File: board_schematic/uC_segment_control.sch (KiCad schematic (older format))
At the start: 61 parts, among them IC1 ATMEGA88PA-P, P1 CONN_02X05

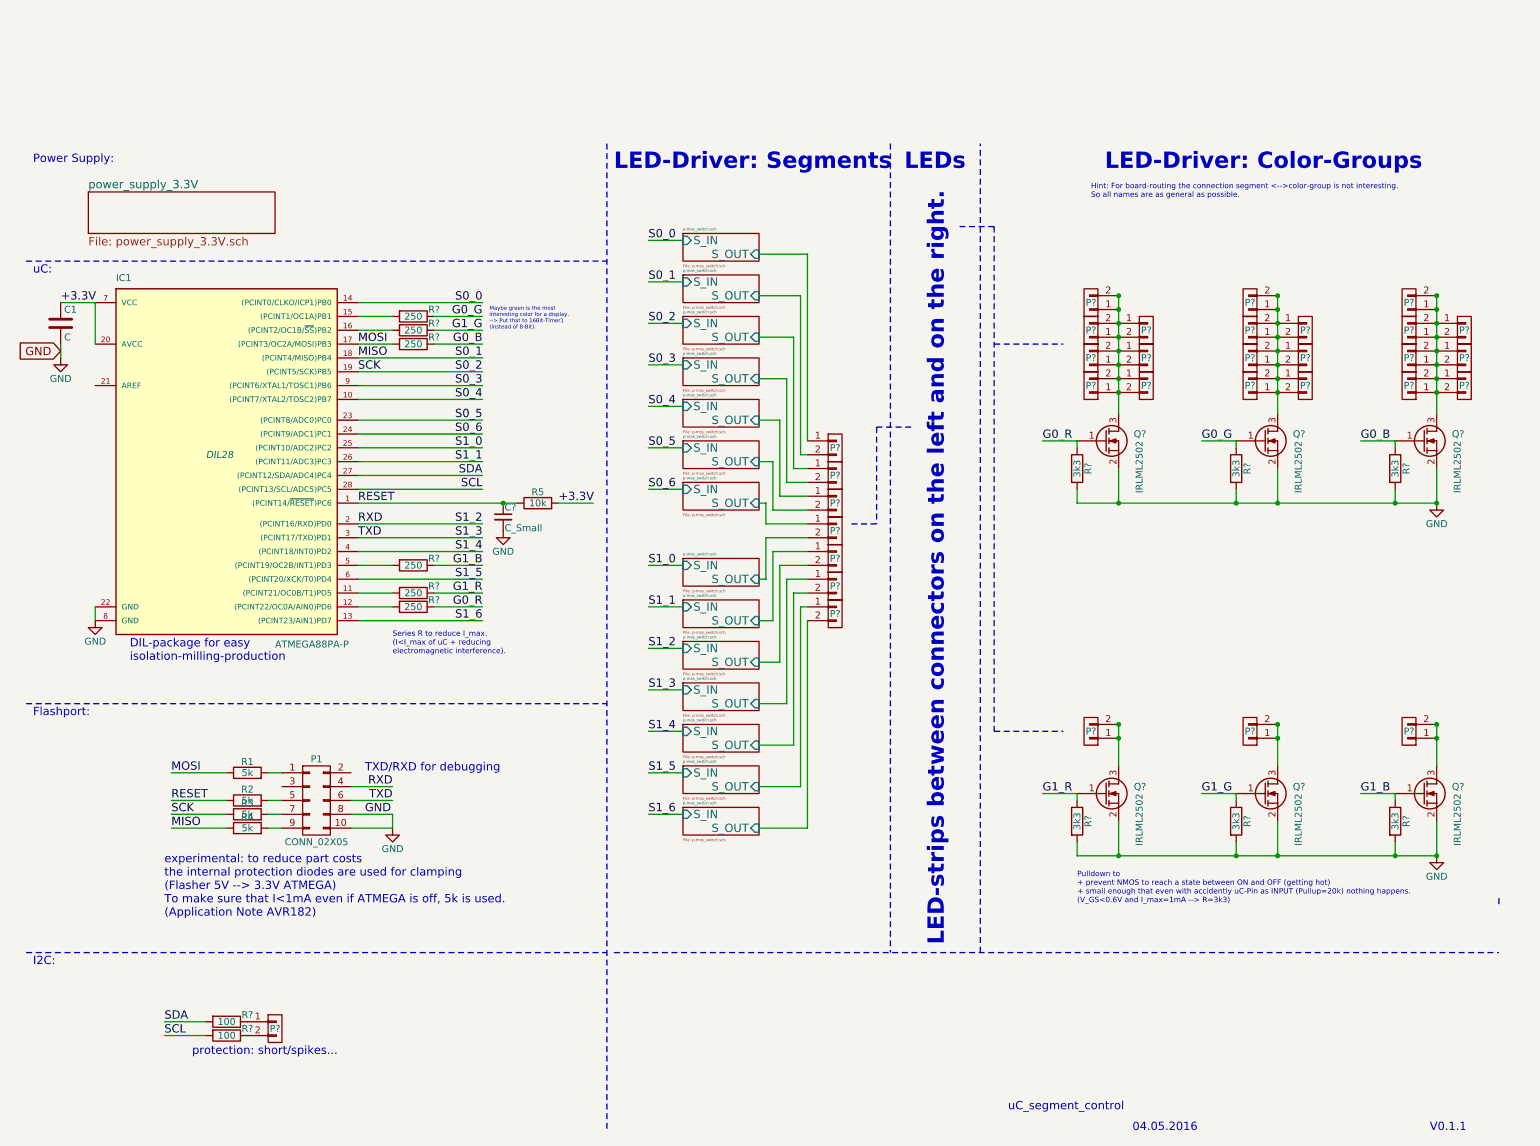
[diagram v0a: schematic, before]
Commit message: V0.2.1: First schematic for BOM
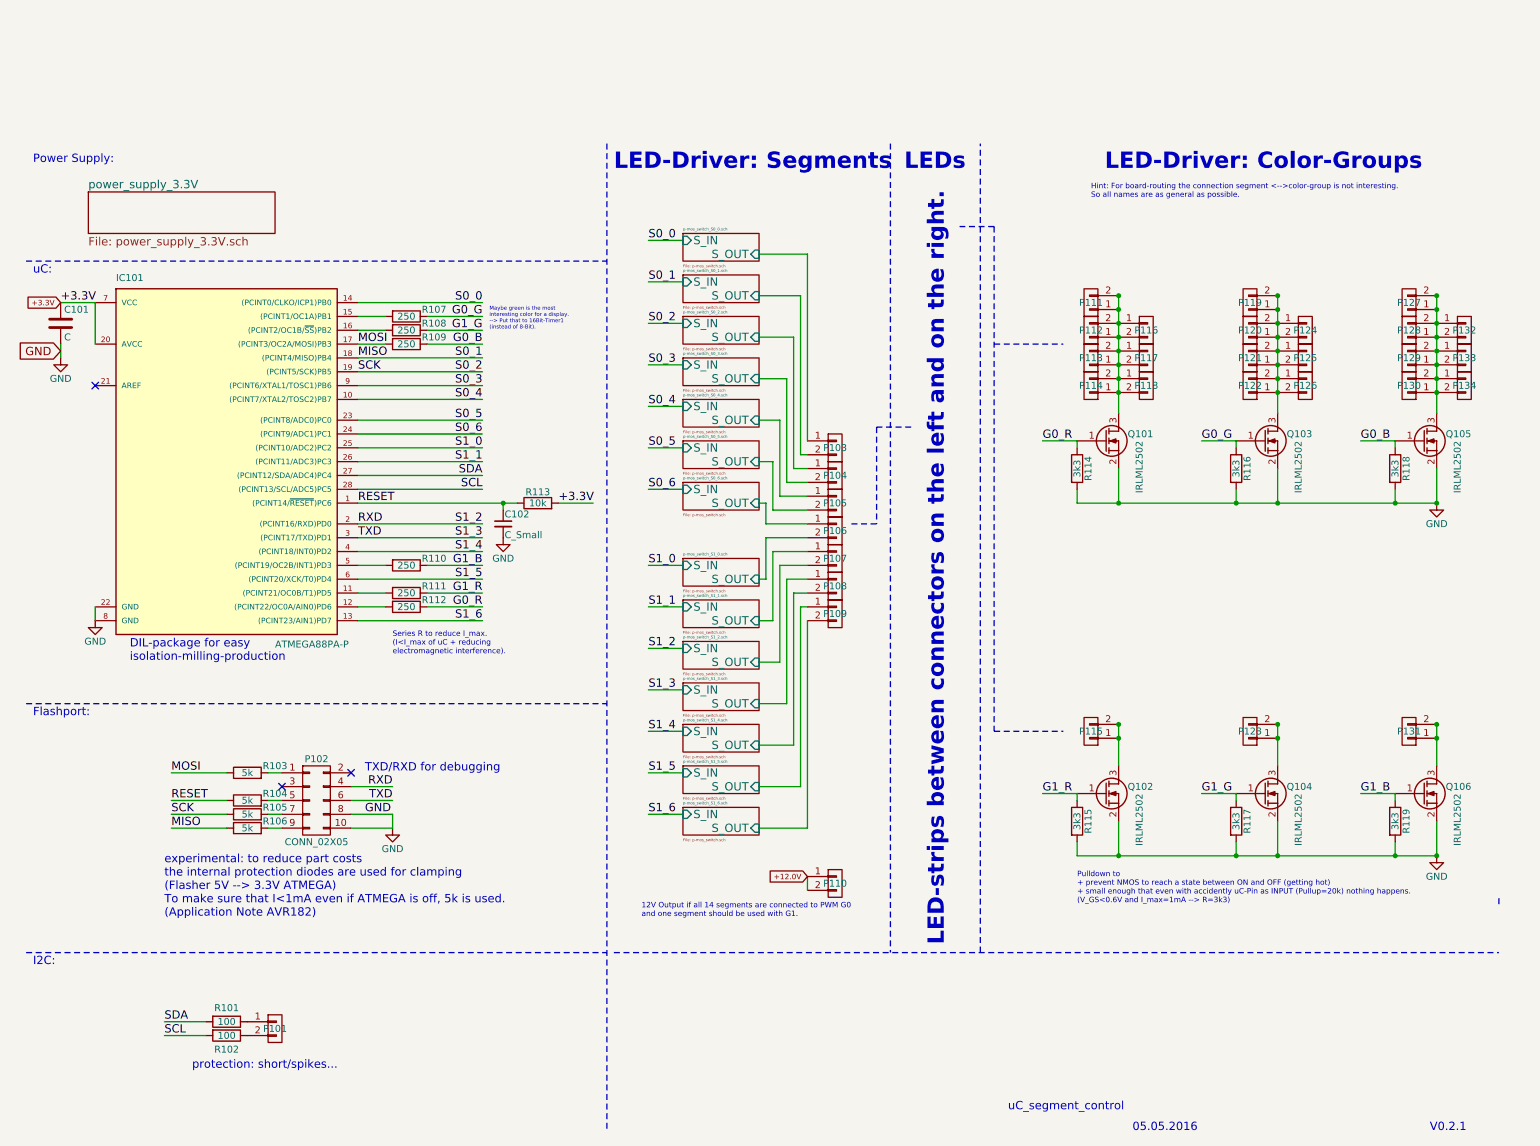
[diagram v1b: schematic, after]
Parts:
- added P110: CONN_01X02, Connect:bornier2, symbol CONN_01X02
- C101: renamed from C1; footprint (none) -> Capacitors_SMD:C_0805_HandSoldering
- C102: renamed from C?; footprint (none) -> Capacitors_SMD:C_0805_HandSoldering
- IC101: renamed from IC1; footprint DIL28 -> Housings_DIP:DIP-28_W7.62mm_LongPads
- P101, P103, P104, P105, P106, P107, P108, P109, P111, P112, P113, P114, P115, P116, P117, P118, P119, P120, P121, P122, P123, P124, P125, P126, P127, P128, P129, P130, P131, P132, P133, P134: renamed from P?; footprint (none) -> Connect:bornier2
- Q101, Q102, Q103, Q104, Q105, Q106: renamed from Q?; footprint (none) -> TO_SOT_Packages_SMD:SOT-23_Handsoldering
- gave numbers to parts that had none: 14
- renumbered P1 to P102, R1 to R103, R2 to R104, R3 to R105, R4 to R106, R5 to R113
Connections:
- net p-mos_switch.sch/S_OUT renamed p-mos_switch_S1_5.sch/S_OUT
- net p-mos_switch.sch/S_OUT renamed p-mos_switch_S1_6.sch/S_OUT
- net p-mos_switch.sch/S_OUT renamed p-mos_switch_S1_3.sch/S_OUT
- net p-mos_switch.sch/S_OUT renamed p-mos_switch_S1_4.sch/S_OUT
- net p-mos_switch.sch/S_OUT renamed p-mos_switch_S1_1.sch/S_OUT
- net p-mos_switch.sch/S_OUT renamed p-mos_switch_S1_2.sch/S_OUT
- net p-mos_switch.sch/S_OUT renamed p-mos_switch_S0_6.sch/S_OUT
- net p-mos_switch.sch/S_OUT renamed p-mos_switch_S1_0.sch/S_OUT
- net p-mos_switch.sch/S_OUT renamed p-mos_switch_S0_4.sch/S_OUT
- net p-mos_switch.sch/S_OUT renamed p-mos_switch_S0_5.sch/S_OUT
- net p-mos_switch.sch/S_OUT renamed p-mos_switch_S0_2.sch/S_OUT
- net p-mos_switch.sch/S_OUT renamed p-mos_switch_S0_3.sch/S_OUT
- net p-mos_switch.sch/S_OUT renamed p-mos_switch_S0_0.sch/S_OUT
- net p-mos_switch.sch/S_OUT renamed p-mos_switch_S0_1.sch/S_OUT
- new net +12.0V: P110.1 (P1), P110.2 (P2)
- no-connect marks 0 -> 3
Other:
- note added: "05.05.2016"
- note added: "12V Output if all 14 segments are connected to PWM G0\nand one segment should be used with G1."
- note added: "V0.2.1"
- note removed: "04.05.2016"
- note removed: "V0.1.1"
- moved on the sheet: C102, R107, R108, R109, R110, R111, R112

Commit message: V0.3.1: First layout
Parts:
- removed P105, P106, P107, P111, P112, P113, P119, P120, P121, P127, P128, P129: CONN_01X02, Connect:bornier2, symbol CONN_01X02
- added P101, P102, P103, P104, P105, P106, P121, P122: CONN_01X03, Connect:AK300-3, symbol CONN_01X03
- added R112, R114: 5k, Resistors_SMD:R_0805_HandSoldering, symbol R
- C101: value C -> 100n
- C102: value C_Small -> 100n
- P107: renamed from P116; footprint Connect:bornier2 -> Connect:AK300-2
- P108: renamed from P117; footprint Connect:bornier2 -> Connect:AK300-2
- P109: renamed from P124; footprint Connect:bornier2 -> Connect:AK300-2
- P110: renamed from P125; footprint Connect:bornier2 -> Connect:AK300-2
- P111: renamed from P132; footprint Connect:bornier2 -> Connect:AK300-2
- P112: renamed from P133; footprint Connect:bornier2 -> Connect:AK300-2
- P113: renamed from P114; footprint Connect:bornier2 -> Connect:AK300-2
- P114: renamed from P118; footprint Connect:bornier2 -> Connect:AK300-2
- P115: renamed from P122; footprint Connect:bornier2 -> Connect:AK300-2
- P116: renamed from P126; footprint Connect:bornier2 -> Connect:AK300-2
- P117: renamed from P130; footprint Connect:bornier2 -> Connect:AK300-2
- P118: renamed from P134; footprint Connect:bornier2 -> Connect:AK300-2
- P119: renamed from P103; footprint Connect:bornier2 -> Connect:AK300-2
- P120: renamed from P104; footprint Connect:bornier2 -> Connect:AK300-2
- P123: renamed from P108; footprint Connect:bornier2 -> Connect:AK300-2
- P124: renamed from P109; footprint Connect:bornier2 -> Connect:AK300-2
- P125: renamed from P115; footprint Connect:bornier2 -> Connect:AK300-2
- P126: renamed from P123; footprint Connect:bornier2 -> Connect:AK300-2
- P127: renamed from P131; footprint Connect:bornier2 -> Connect:AK300-2
- P129: renamed from P110; footprint Connect:bornier2 -> Connect:AK300-2
- P130: renamed from P101; footprint Connect:bornier2 -> Connect:AK300-2
- R101: renamed from R107; value 250 -> 270
- R102: renamed from R108; value 250 -> 270
- R103: renamed from R109; value 250 -> 270
- R108: renamed from R110; value 250 -> 270
- R109: renamed from R111; value 250 -> 270
- R110: renamed from R112; value 250 -> 270
- renumbered P102 to P128, Q103 to Q102, Q105 to Q103, Q102 to Q104, Q104 to Q105, R114 to R104, R116 to R105, R118 to R106, R113 to R107, R103 to R111, R104 to R113, R105 to R115, R115 to R116, R119 to R118, R106 to R119, R101 to R120, R102 to R121
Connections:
- net RXD: now also R112.2; no longer P128.4 (P4)
- net S1_3: now also R114.2; no longer P128.6 (P6)
- net p-mos_switch_S0_4.sch/S_OUT: now also P121.1 (P1)
- net p-mos_switch_S0_5.sch/S_OUT: now also P121.2 (P2)
- net p-mos_switch_S0_6.sch/S_OUT: now also P121.3 (P3)
- net p-mos_switch_S1_0.sch/S_OUT: now also P122.1 (P1)
- net p-mos_switch_S1_1.sch/S_OUT: now also P122.2 (P2)
- net p-mos_switch_S1_2.sch/S_OUT: now also P122.3 (P3)
- net at P107.1 (P1), P107.2 (P2), P108.1 (P1)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: now also P101.1 (P1), P101.2 (P2), P101.3 (P3), P102.1 (P1), P102.2 (P2), P102.3 (P3)
- net at P109.1 (P1), P109.2 (P2), P110.1 (P1)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: now also P103.1 (P1), P103.2 (P2), P103.3 (P3), P104.1 (P1), P104.2 (P2), P104.3 (P3)
- net at P111.1 (P1), P111.2 (P2), P112.1 (P1)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: now also P105.1 (P1), P105.2 (P2), P105.3 (P3), P106.1 (P1), P106.2 (P2), P106.3 (P3)
- new net: P128.4 (P4), R112.1
- new net: P128.6 (P6), R114.1
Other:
- note removed: "05.05.2016"
- note removed: "V0.2.1"
- note removed: "uC_segment_control"
- moved on the sheet: P107, P109, P111

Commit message: V0.4.1 bigger pads footprint flashport for better milling. Case added.
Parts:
- P128: footprint Connect:IDC_Header_Straight_10pins -> project_footprints:IDC_Header_Straight_10pins_0.6_clearance
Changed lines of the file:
@@
 Sheet 1 16
 Title "uC_segment_control"
-Date "2016-05-12"
-Rev "V0.3.1"
+Date "2016-05-19"
+Rev "V0.4.1"
 Comp ""
 Comment1 ""
@@
 F 0 "P128" H 2600 5550 50  0000 C CNN
 F 1 "CONN_02X05" H 2600 4950 50  0000 C CNN
-F 2 "Connect:IDC_Header_Straight_10pins" H 2600 4050 50  0001 C CNN
+F 2 "project_footprints:IDC_Header_Straight_10pins_0.6_clearance" H 2600 4050 50  0001 C CNN
 F 3 "" H 2600 4050 50  0000 C CNN
 	1    2600 5250
